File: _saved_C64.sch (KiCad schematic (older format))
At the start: 239 parts, among them CN1 Keyboard, CN10 JP2E, CN2 USERPORT-C64-EDGE, CN3 CASSETTEPORT, CN4 DIN6, CN5 DIN5, CN6 EXPANSIONPORT, CN7 DIN7, CN8 CONTROL_PORT, CN9 CONTROL_PORT, J1 Conn_01x01, J2 Conn_01x01, J3 Conn_01x01, Q1 TIP29B, Q2 2N4401, Q3 2N3904, Q4 PN2222, Q5 PN2222, Q6 PN2222, Q7 PN2222, Q8 PN2222, SW1 DPDT_SWITCH, U1 6526, U10 4164, U11 4164, U12 4164, U13 SN74257N, U14 SN74258N, U15 SN74139N, U16 4066, U17 C64PLA, U18 6581, U19 6569, U2 6526, U20 556DIGITAL, U21 4164, U22 4164, U23 4164, U24 4164, U25 SN74257N, U26 74373N, U27 SN7408N, U28 4066, U29 SN7474N, U3 2364, U30 SN74193N, U31 SN74629, U32 MC4044, U33 7402, U34 74LS175, U4 2364, U5 2332, U6 2114, U7 6510, U8 SN7406NN, U9 4164, Y1 17.73 MHz

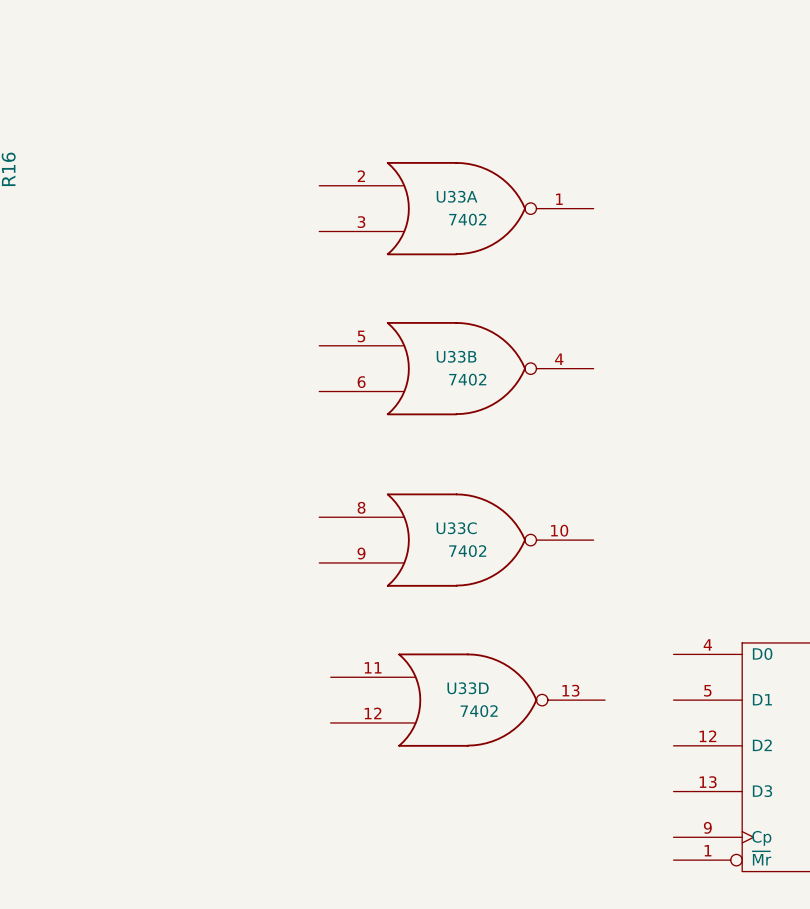
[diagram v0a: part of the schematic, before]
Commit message: added schematic symbols for U33 and U34
u33 needs some edit work before connections in schematic can be made
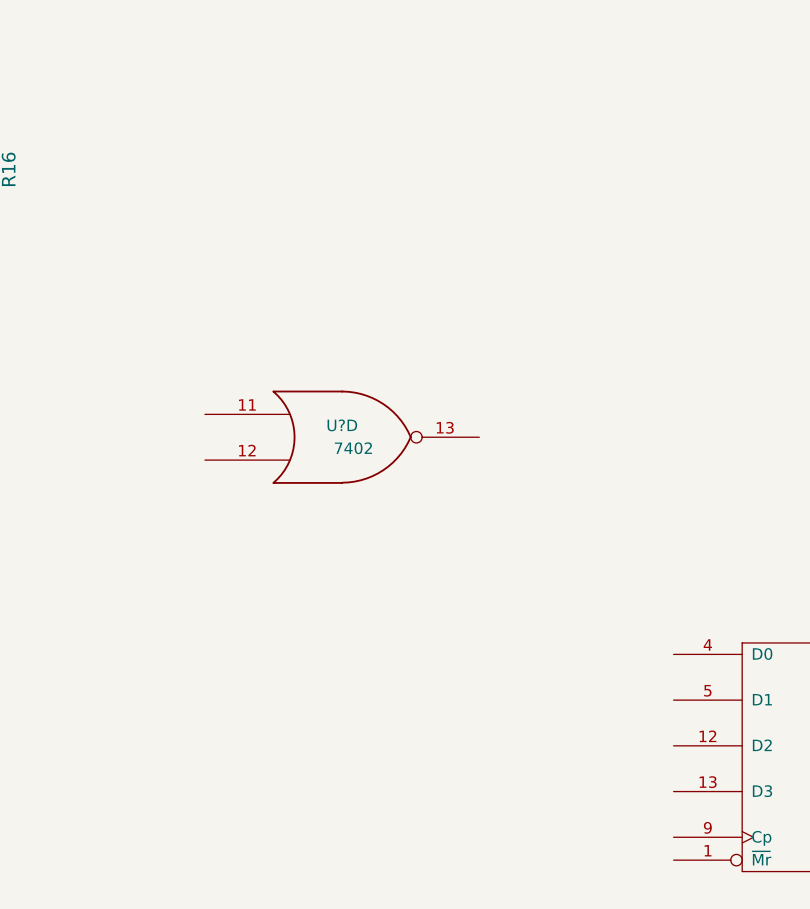
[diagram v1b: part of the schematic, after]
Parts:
- removed U33: 7402, symbol 7402
- added U?: 7402, symbol 7402
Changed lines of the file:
@@
 LIBS:BRIDGE_RECTIFIER
 LIBS:74ls175
+LIBS:74ls02
 LIBS:C64-cache
 EELAYER 25 0
@@
 +9V
 $Comp
-L 7402 U33
-U 1 1 5A9BA328
-P 22150 18200
-F 0 "U33" H 22150 18250 50  0000 C CNN
-F 1 "7402" H 22200 18150 50  0000 C CNN
-F 2 "" H 22150 18200 50  0001 C CNN
-F 3 "" H 22150 18200 50  0001 C CNN
-	1    22150 18200
-	1    0    0    -1
-$EndComp
-$Comp
-L 7402 U33
-U 2 1 5A9BA5FD
-P 22150 18900
-F 0 "U33" H 22150 18950 50  0000 C CNN
-F 1 "7402" H 22200 18850 50  0000 C CNN
-F 2 "" H 22150 18900 50  0001 C CNN
-F 3 "" H 22150 18900 50  0001 C CNN
-	2    22150 18900
-	1    0    0    -1
-$EndComp
-$Comp
-L 7402 U33
-U 3 1 5A9BA886
-P 22150 19650
-F 0 "U33" H 22150 19700 50  0000 C CNN
-F 1 "7402" H 22200 19600 50  0000 C CNN
-F 2 "" H 22150 19650 50  0001 C CNN
-F 3 "" H 22150 19650 50  0001 C CNN
-	3    22150 19650
-	1    0    0    -1
-$EndComp
-$Comp
-L 7402 U33
-U 4 1 5A9BAB81
-P 22200 20350
-F 0 "U33" H 22200 20400 50  0000 C CNN
-F 1 "7402" H 22250 20300 50  0000 C CNN
-F 2 "" H 22200 20350 50  0001 C CNN
-F 3 "" H 22200 20350 50  0001 C CNN
-	4    22200 20350
-	1    0    0    -1
-$EndComp
-$Comp
 L 74LS175 U34
 U 1 1 5A9C0D5D
@@
 Text Label 28950 2550 0    10   ~ 0
 GND
+$Comp
+L 7402 U?
+U 4 1 5A9E645B
+P 21650 19200
+F 0 "U?" H 21650 19250 50  0000 C CNN
+F 1 "7402" H 21700 19150 50  0000 C CNN
+F 2 "" H 21650 19200 50  0001 C CNN
+F 3 "" H 21650 19200 50  0001 C CNN
+	4    21650 19200
+	1    0    0    -1
+$EndComp
 $EndSCHEMATC
